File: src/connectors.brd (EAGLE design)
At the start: 37.8 x 13.4 mm, 11 parts, among them CON1 CON-4P-TABS-JST_GH-RA, CON11 PINHEAD_1X03-2, CON12 PINHEAD_1X03-2, CON3 CON-4P-TABS-JST_GH-RA, IC6 TJA1051-HVSON8, IC8 TPD3S014DBVR-SOT23-6

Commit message: Updates here and there
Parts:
- moved CON11 0.90 mm to (16.8, -3.90)
- moved CON12 0.90 mm to (-16.8, -3.90)
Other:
- board size 37.8 x 13.4 mm -> 36 x 13.4 mm
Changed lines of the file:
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@@
 <setting verticaltext="up"/>
 </settings>
-<grid distance="0.1" unitdist="mm" unit="mm" style="lines" multiple="1" display="yes" altdistance="5" altunitdist="mil" altunit="mil"/>
+<grid distance="0.3" unitdist="mm" unit="mm" style="lines" multiple="1" display="yes" altdistance="5" altunitdist="mil" altunit="mil"/>
 <layers>
 <layer number="1" name="Top" color="4" fill="1" visible="yes" active="yes"/>
@@
 <layer number="14" name="Route14" color="22" fill="1" visible="no" active="no"/>
 <layer number="15" name="Route15" color="23" fill="1" visible="no" active="no"/>
-<layer number="16" name="Bottom" color="1" fill="1" visible="yes" active="yes"/>
+<layer number="16" name="Bottom" color="1" fill="1" visible="no" active="yes"/>
 <layer number="17" name="Pads" color="2" fill="1" visible="yes" active="yes"/>
 <layer number="18" name="Vias" color="2" fill="1" visible="yes" active="yes"/>
@@
 <layer number="20" name="Dimension" color="24" fill="1" visible="yes" active="yes"/>
 <layer number="21" name="tPlace" color="7" fill="1" visible="yes" active="yes"/>
-<layer number="22" name="bPlace" color="7" fill="1" visible="yes" active="yes"/>
+<layer number="22" name="bPlace" color="7" fill="1" visible="no" active="yes"/>
 <layer number="23" name="tOrigins" color="15" fill="1" visible="yes" active="yes"/>
-<layer number="24" name="bOrigins" color="15" fill="1" visible="yes" active="yes"/>
+<layer number="24" name="bOrigins" color="15" fill="1" visible="no" active="yes"/>
 <layer number="25" name="tNames" color="7" fill="1" visible="yes" active="yes"/>
-<layer number="26" name="bNames" color="7" fill="1" visible="yes" active="yes"/>
+<layer number="26" name="bNames" color="7" fill="1" visible="no" active="yes"/>
 <layer number="27" name="tValues" color="7" fill="1" visible="no" active="yes"/>
 <layer number="28" name="bValues" color="7" fill="1" visible="no" active="yes"/>
@@
 <layer number="50" name="dxf" color="7" fill="1" visible="no" active="no"/>
 <layer number="51" name="tDocu" color="7" fill="1" visible="yes" active="yes"/>
-<layer number="52" name="bDocu" color="7" fill="1" visible="yes" active="yes"/>
+<layer number="52" name="bDocu" color="7" fill="1" visible="no" active="yes"/>
 <layer number="53" name="tGND_GNDA" color="7" fill="9" visible="no" active="no"/>
 <layer number="54" name="bGND_GNDA" color="1" fill="9" visible="no" active="no"/>
@@
 </layers>
 <board>
-<fusionsync huburn="a.cGVyc29uYWw6dWUyYWE4ZDY4" projecturn="a.cGVyc29uYWw6dWUyYWE4ZDY4IzIwMjAwOTI1MzM2NDYxMjgx" f3durn="urn:adsk.wipprod:dm.lineage:pbb1l4fuQAGy4r_gEChu-w" pcbguid="" lastpulledtime="" lastsyncedchangeguid="" latestrevisionid="46bfaa87-77a5-4bb5-bbbf-92cb329495d3" lastsyncedrevisionid="46bfaa87-77a5-4bb5-bbbf-92cb329495d3" lastboardhashguid="8e5156ea-7f44-40c5-9889-4eb4bba22418" lastpushedtime="2020-10-07T14:29:08Z" linktopcb3d="true"/>
+<fusionsync huburn="a.cGVyc29uYWw6dWUyYWE4ZDY4" projecturn="a.cGVyc29uYWw6dWUyYWE4ZDY4IzIwMjAwOTI1MzM2NDYxMjgx" f3durn="urn:adsk.wipprod:dm.lineage:5f-RR5beSAqgs6k1iF_brA" pcbguid="" lastpulledtime="" lastsyncedchangeguid="" latestrevisionid="91c3f639-02cc-4b84-a14b-e3aaad1c6eab" lastsyncedrevisionid="91c3f639-02cc-4b84-a14b-e3aaad1c6eab" lastboardhashguid="354a8440-501e-4556-71f2-56a415103d28" lastpushedtime="2020-10-31T23:22:11Z" linktopcb3d="false"/>
 <plain>
 <wire x1="5.5" y1="1.1" x2="5.5" y2="0.1" width="0.1524" layer="138"/>
 <wire x1="5" y1="0.6" x2="6" y2="0.6" width="0.1524" layer="138"/>
-<wire x1="-15.1" y1="6.3" x2="-15.1" y2="3.65" width="0.01" layer="20"/>
-<wire x1="-15.1" y1="3.65" x2="-17.35" y2="1.4" width="0.01" layer="20" curve="-90"/>
-<wire x1="-17.35" y1="1.4" x2="-18.9" y2="1.4" width="0.01" layer="20"/>
-<wire x1="-18.9" y1="1.4" x2="-18.9" y2="-7.1" width="0.01" layer="20"/>
-<wire x1="-18.9" y1="-7.1" x2="-15" y2="-7.1" width="0.01" layer="20"/>
-<wire x1="14.8" y1="-7.1" x2="14.8" y2="-1" width="0.01" layer="20"/>
-<wire x1="14.8" y1="-1" x2="13.8" y2="0" width="0.01" layer="20" curve="90"/>
-<wire x1="13.8" y1="0" x2="-14" y2="0" width="0.01" layer="20"/>
-<wire x1="-14" y1="0" x2="-15" y2="-1" width="0.01" layer="20" curve="90"/>
-<wire x1="-15" y1="-1" x2="-15" y2="-7.1" width="0.01" layer="20"/>
-<wire x1="-15.1" y1="6.3" x2="15.1" y2="6.3" width="0.01" layer="20"/>
-<wire x1="15.1" y1="6.3" x2="15.1" y2="3.65" width="0.01" layer="20"/>
-<wire x1="15.1" y1="3.65" x2="17.35" y2="1.4" width="0.01" layer="20" curve="90"/>
-<wire x1="17.35" y1="1.4" x2="18.9" y2="1.4" width="0.01" layer="20"/>
-<wire x1="18.9" y1="1.4" x2="18.9" y2="-7.1" width="0.01" layer="20"/>
-<wire x1="18.9" y1="-7.1" x2="14.8" y2="-7.1" width="0.01" layer="20"/>
+<wire x1="17" y1="-7.1" x2="15.6" y2="-7.1" width="0.01" layer="20"/>
+<wire x1="15.6" y1="-7.1" x2="14.6" y2="-6.1" width="0.01" layer="20" curve="-90"/>
+<wire x1="14.6" y1="-6.1" x2="14.6" y2="-1" width="0.01" layer="20"/>
+<wire x1="14.6" y1="-1" x2="13.6" y2="0" width="0.01" layer="20" curve="90"/>
+<wire x1="13.6" y1="0" x2="-13.6" y2="0" width="0.01" layer="20"/>
+<wire x1="-13.6" y1="0" x2="-14.6" y2="-1" width="0.01" layer="20" curve="90"/>
+<wire x1="-14.6" y1="-1" x2="-14.6" y2="-6.1" width="0.01" layer="20"/>
+<wire x1="-14.6" y1="-6.1" x2="-15.6" y2="-7.1" width="0.01" layer="20" curve="-90"/>
+<wire x1="-15.6" y1="-7.1" x2="-17" y2="-7.1" width="0.01" layer="20"/>
+<wire x1="-17" y1="-7.1" x2="-18" y2="-6.1" width="0.01" layer="20" curve="-90"/>
+<wire x1="-18" y1="-6.1" x2="-18" y2="5.3" width="0.01" layer="20"/>
+<wire x1="-18" y1="5.3" x2="-17" y2="6.3" width="0.01" layer="20" curve="-90"/>
+<wire x1="-17" y1="6.3" x2="17" y2="6.3" width="0.01" layer="20"/>
+<wire x1="17" y1="6.3" x2="18" y2="5.3" width="0.01" layer="20" curve="-90"/>
+<wire x1="18" y1="5.3" x2="18" y2="-6.1" width="0.01" layer="20"/>
+<wire x1="18" y1="-6.1" x2="17" y2="-7.1" width="0.01" layer="20" curve="-90"/>
 </plain>
 <attributes>
@@
 <attribute name="VOLTAGE" value="6.3V" x="-7" y="5.3" size="1.778" layer="27" rot="R90" display="off"/>
 </element>
-<element name="CON11" library="pinhead" library_urn="urn:adsk.eagle:library:2540341" package="1X03-PTH-2" package3d_urn="urn:adsk.eagle:package:4854341/3" value="PINHEAD_1X03-2" x="17.7" y="-3.9" smashed="yes" rot="R270">
-<attribute name="NAME" x="19.3" y="-3.9" size="1" layer="25" font="vector" ratio="15" rot="R270" align="center"/>
-</element>
-<element name="CON12" library="pinhead" library_urn="urn:adsk.eagle:library:2540341" package="1X03-PTH-2" package3d_urn="urn:adsk.eagle:package:4854341/3" value="PINHEAD_1X03-2" x="-17.7" y="-3.9" smashed="yes" rot="R90">
-<attribute name="NAME" x="-19.3" y="-3.9" size="1" layer="25" font="vector" ratio="15" rot="R90" align="center"/>
+<element name="CON11" library="pinhead" library_urn="urn:adsk.eagle:library:2540341" package="1X03-PTH-2" package3d_urn="urn:adsk.eagle:package:4854341/3" value="PINHEAD_1X03-2" x="16.8" y="-3.9" smashed="yes" rot="R270">
+<attribute name="NAME" x="18.4" y="-3.9" size="1" layer="25" font="vector" ratio="15" rot="R270" align="center"/>
+</element>
+<element name="CON12" library="pinhead" library_urn="urn:adsk.eagle:library:2540341" package="1X03-PTH-2" package3d_urn="urn:adsk.eagle:package:4854341/3" value="PINHEAD_1X03-2" x="-16.8" y="-3.9" smashed="yes" rot="R90">
+<attribute name="NAME" x="-18.4" y="-3.9" size="1" layer="25" font="vector" ratio="15" rot="R90" align="center"/>
 </element>
 </elements>

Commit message: connectors PCB routing effort
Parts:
- removed CON11, CON12: PINHEAD_1X03-2, pinhead:1X03-PTH-2
- added CON2: CON-4P-TABS-JST_GH-RA, Connectors:JST_GH-4P-RA
- added CON4: PINHEAD_1X04-2, pinhead:1X04-PTH-2
- CON3: value CON-4P-TABS-JST_GH-RA -> PINHEAD_1X04-2; device Connectors:JST_GH-4P-RA -> pinhead:1X04-PTH-2
- moved C84 83.5 mm to (16.9, 78.7)
- moved C28 79.2 mm to (15.7, 78.5), turned to 270 degrees
- moved IC8 78.6 mm to (15.5, 75.6), turned to 180 degrees
- moved C53 78.2 mm to (12.5, 79.1), turned to 180 degrees
- moved C29 77.9 mm to (14.4, 78.5), turned to 270 degrees
- moved IC6 74.0 mm to (11.0, 76.5), turned to 0 degrees
- moved CON1 74.0 mm to (-4.50, 78.2)
- moved C11 71.8 mm to (11.2, 74.3), turned to 180 degrees
- moved CON3 66.7 mm to (16.8, 69.8), turned to 270 degrees
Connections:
- net CAN1_RX: now also CON3.3
- net CAN1_TX: now also CON3.4
- net CAN1_VDD: now also CON2.1; no longer CON3.1
- net GND: now also CON2.4, CON2.M$0, CON2.M$1, CON3.2; no longer CON3.4, CON3.M$0, CON3.M$1
- net N$23: now also CON2.2; no longer CON3.2
- net N$25: now also CON2.3; no longer CON3.3
- net VDD_5V: now also CON3.1
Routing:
- net N$25: track 0.00 -> 26.5 mm, vias 0 -> 2
- net N$23: track 0.00 -> 22.2 mm, vias 0 -> 2
- net CAN1_TX: track 0.00 -> 17.9 mm, vias 0 -> 2
- net CAN1_RX: track 0.00 -> 13.6 mm, vias 0 -> 2
- net VDD_5V: track 0.00 -> 11.6 mm, vias 0 -> 5
- net CAN1_VDD: track 0.00 -> 6.51 mm, vias 0 -> 12
- net GND: track 0.00 -> 2.92 mm, vias 0 -> 17
- added copper zone on layer 1, net CAN1_VDD
- added copper zone on layer 16, net CAN1_VDD
- added copper zone on layer 1, net GND
- added copper zone on layer 16, net GND
- added copper zone on layer 1, net VDD_5V
- added copper zone on layer 16, net VDD_5V
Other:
- board size 36 x 13.4 mm -> 36 x 14.4 mm

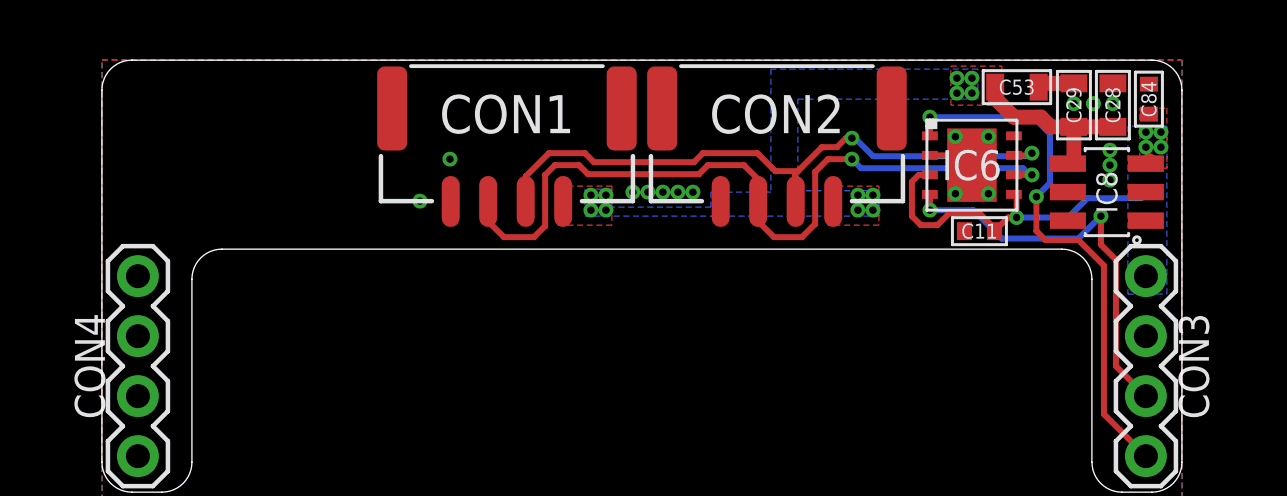
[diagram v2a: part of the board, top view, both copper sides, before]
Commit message: connectors pcb adjustments
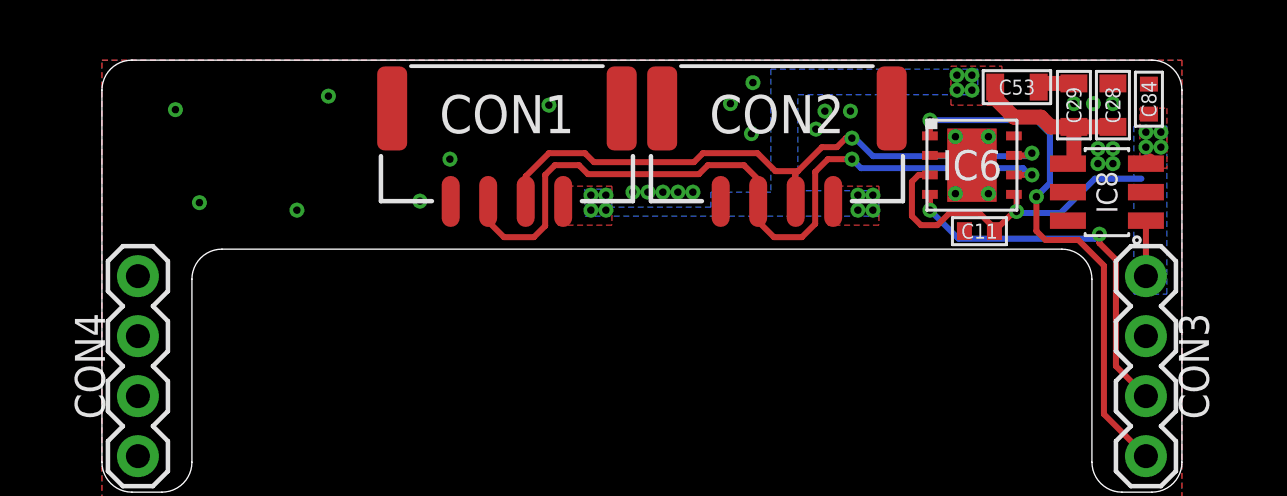
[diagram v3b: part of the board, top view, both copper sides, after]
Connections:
- removed net BEC_EN: IC8.1
- net VDD_5V: now also IC8.1
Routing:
- net VDD_5V: track 11.6 -> 13.6 mm
- net CAN1_RX: track 13.6 -> 12.7 mm
- net GND: track 2.92 -> 2.76 mm, vias 17 -> 29
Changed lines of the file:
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@@
 <vertex x="-18" y="65"/>
 </polygon>
-<wire x1="-7.29" y1="75.19" x2="-7.4" y2="75.3" width="0.2" layer="1"/>
 <via x="-7.4" y="75.3" extent="1-16" drill="0.25" diameter="0.5"/>
 <via x="-6.4" y="76.7" extent="1-16" drill="0.25" diameter="0.5"/>
@@
 <wire x1="9.6" y1="76.825" x2="10.675" y2="76.825" width="0.2" layer="1"/>
 <wire x1="10.675" y1="76.825" x2="11" y2="76.5" width="0.2" layer="1"/>
-<via x="15.6" y="77" extent="1-16" drill="0.25" diameter="0.5"/>
-<via x="15.6" y="76.5" extent="1-16" drill="0.25" diameter="0.5"/>
-<via x="15.6" y="76" extent="1-16" drill="0.25" diameter="0.5"/>
+<via x="15.7" y="77.05" extent="1-16" drill="0.25" diameter="0.5"/>
+<via x="15.7" y="76.55" extent="1-16" drill="0.25" diameter="0.5"/>
+<via x="15.2" y="76.55" extent="1-16" drill="0.25" diameter="0.5"/>
 <via x="15.7" y="78.55" extent="1-16" drill="0.25" diameter="0.5"/>
 <via x="15.05" y="78.55" extent="1-16" drill="0.25" diameter="0.5"/>
@@
 <via x="10.45" y="77.45" extent="1-16" drill="0.25" diameter="0.5"/>
 <via x="11.55" y="77.45" extent="1-16" drill="0.25" diameter="0.5"/>
-<wire x1="13.225" y1="79.1" x2="11.55" y2="77.45" width="0" layer="19" extent="1-1"/>
-<wire x1="16.8" y1="70.8" x2="16.8" y2="75.6" width="0" layer="19" extent="1-1"/>
+<via x="15.2" y="77.05" extent="1-16" drill="0.25" diameter="0.5"/>
+<via x="-10.45" y="78.8" extent="1-16" drill="0.25" diameter="0.5"/>
+<via x="-15.55" y="78.35" extent="1-16" drill="0.25" diameter="0.5"/>
+<via x="-14.75" y="75.25" extent="1-16" drill="0.25" diameter="0.5"/>
+<via x="-11.5" y="75" extent="1-16" drill="0.25" diameter="0.5"/>
+<via x="-3.1" y="78.5" extent="1-16" drill="0.25" diameter="0.5"/>
+<via x="3.7" y="79.25" extent="1-16" drill="0.25" diameter="0.5"/>
+<via x="2.95" y="78.55" extent="1-16" drill="0.25" diameter="0.5"/>
+<via x="6.1" y="78.3" extent="1-16" drill="0.25" diameter="0.5"/>
+<via x="5.8" y="77.7" extent="1-16" drill="0.25" diameter="0.5"/>
+<via x="6.95" y="78.3" extent="1-16" drill="0.25" diameter="0.5"/>
+<via x="3.65" y="77.55" extent="1-16" drill="0.25" diameter="0.5"/>
 </signal>
 <signal name="CAN1_TX">
 <contactref element="IC6" pad="1"/>
 <contactref element="CON3" pad="4"/>
-<wire x1="9.6" y1="77.475" x2="9.6" y2="78.1" width="0.2" layer="1"/>
-<via x="9.6" y="78.1" extent="1-16" drill="0.25" diameter="0.5"/>
+<wire x1="9.6" y1="77.475" x2="9.6" y2="78" width="0.2" layer="1"/>
+<via x="9.6" y="78" extent="1-16" drill="0.25" diameter="0.5"/>
 <wire x1="16.8" y1="66.8" x2="15.4" y2="68.2" width="0.2" layer="1"/>
 <wire x1="15.4" y1="68.2" x2="15.4" y2="73.15259375" width="0.2" layer="1"/>
@@
 <via x="13.15" y="75.45" extent="1-16" drill="0.25" diameter="0.5"/>
 <wire x1="13.15" y1="75.45" x2="13.6" y2="75.9" width="0.2" layer="16"/>
-<wire x1="13.05" y1="78.1" x2="9.6" y2="78.1" width="0.2" layer="16"/>
+<wire x1="13.15" y1="78" x2="9.6" y2="78" width="0.2" layer="16"/>
 <wire x1="13.6" y1="75.9" x2="13.6" y2="77.55" width="0.2" layer="16"/>
-<wire x1="13.6" y1="77.55" x2="13.05" y2="78.1" width="0.2" layer="16"/>
+<wire x1="13.6" y1="77.55" x2="13.15" y2="78" width="0.2" layer="16"/>
 </signal>
 <signal name="CAN1_RX">
@@
 <via x="9.6" y="75" extent="1-16" drill="0.25" diameter="0.5"/>
 <wire x1="16.8" y1="68.8" x2="15.8" y2="69.8" width="0.2" layer="1"/>
-<wire x1="15.8" y1="73.35" x2="15.3" y2="73.85" width="0.2" layer="1"/>
-<wire x1="15.3" y1="73.85" x2="15.3" y2="74.8" width="0.2" layer="1"/>
-<via x="15.3" y="74.8" extent="1-16" drill="0.25" diameter="0.5"/>
+<wire x1="15.8" y1="73.35" x2="15.25" y2="73.9" width="0.2" layer="1"/>
+<wire x1="15.25" y1="73.9" x2="15.25" y2="74.2" width="0.2" layer="1"/>
+<via x="15.25" y="74.2" extent="1-16" drill="0.25" diameter="0.5"/>
 <wire x1="15.8" y1="69.8" x2="15.8" y2="73.35" width="0.2" layer="1"/>
-<wire x1="15.3" y1="74.8" x2="14.55" y2="74.05" width="0.2" layer="16"/>
-<wire x1="14.55" y1="74.05" x2="12" y2="74.05" width="0.2" layer="16"/>
-<wire x1="12" y1="74.05" x2="11.05" y2="75" width="0.2" layer="16"/>
-<wire x1="11.05" y1="75" x2="9.6" y2="75" width="0.2" layer="16"/>
+<wire x1="15.25" y1="74.2" x2="15.1" y2="74.05" width="0.2" layer="16"/>
+<wire x1="15.1" y1="74.05" x2="10.55" y2="74.05" width="0.2" layer="16"/>
+<wire x1="10.55" y1="74.05" x2="9.6" y2="75" width="0.2" layer="16"/>
 </signal>
 <signal name="N$23">
@@
 <polygon width="0.2" layer="16" thermals="no">
 <vertex x="17.5" y="77.8"/>
-<vertex x="16.2" y="77.8"/>
-<vertex x="16.2" y="72.2"/>
+<vertex x="16.4" y="77.8"/>
+<vertex x="16.4" y="72.2"/>
 <vertex x="17.5" y="72.2"/>
 </polygon>
@@
 <wire x1="10.25" y1="74.9" x2="11.25" y2="74.9" width="0.2" layer="1"/>
 <wire x1="11.75" y1="74.3" x2="11.85" y2="74.3" width="0.2" layer="1"/>
-<via x="12.4878875" y="74.755" extent="1-16" drill="0.25" diameter="0.5"/>
+<via x="12.4878875" y="74.955" extent="1-16" drill="0.25" diameter="0.5"/>
 <wire x1="11.25" y1="74.9" x2="11.85" y2="74.3" width="0.2" layer="1"/>
-<wire x1="11.75" y1="74.3" x2="12.205" y2="74.755" width="0.2" layer="1"/>
-<wire x1="12.205" y1="74.755" x2="12.4878875" y2="74.755" width="0.2" layer="1"/>
+<wire x1="11.75" y1="74.3" x2="12.405" y2="74.955" width="0.2" layer="1"/>
+<wire x1="12.405" y1="74.955" x2="12.4878875" y2="74.955" width="0.2" layer="1"/>
 <wire x1="12.4" y1="75.525" x2="12.4878875" y2="75.4371125" width="0.2" layer="1"/>
-<wire x1="12.4878875" y1="75.4371125" x2="12.4878875" y2="74.755" width="0.2" layer="1"/>
-<wire x1="12.4878875" y1="74.755" x2="14.205" y2="74.755" width="0.2" layer="16"/>
-<wire x1="14.205" y1="74.755" x2="14.85" y2="75.4" width="0.2" layer="16"/>
-<wire x1="14.85" y1="75.4" x2="16.65" y2="75.4" width="0.2" layer="16"/>
+<wire x1="12.4878875" y1="75.4371125" x2="12.4878875" y2="74.955" width="0.2" layer="1"/>
+<wire x1="12.4878875" y1="74.955" x2="12.5378875" y2="74.905" width="0.2" layer="16"/>
+<wire x1="13.955" y1="74.905" x2="12.5378875" y2="74.905" width="0.2" layer="16"/>
+<wire x1="13.955" y1="74.905" x2="15.1" y2="76.05" width="0.2" layer="16"/>
+<wire x1="15.1" y1="76.05" x2="16.65" y2="76.05" width="0.2" layer="16"/>
+<contactref element="IC8" pad="1"/>
+<wire x1="16.8" y1="74.65" x2="16.8" y2="72.8" width="0.2" layer="1"/>
 </signal>
 <signal name="CAN1_VDD">
@@
 <vertex x="7.9" y="75.65"/>
 <vertex x="5.2" y="75.65"/>
-<vertex x="5.2" y="78.7"/>
-<vertex x="11.2" y="78.7"/>
+<vertex x="5.2" y="78.85"/>
+<vertex x="11.2" y="78.85"/>
 <vertex x="11.2" y="79.7"/>
 <vertex x="4.3" y="79.7"/>
@@
 <vertex x="12" y="79.8"/>
 </polygon>
-<via x="11" y="78.9" extent="1-16" drill="0.25" diameter="0.5"/>
-<via x="10.5" y="78.9" extent="1-16" drill="0.25" diameter="0.5"/>
-<via x="11" y="79.4" extent="1-16" drill="0.25" diameter="0.5"/>
-<via x="10.5" y="79.4" extent="1-16" drill="0.25" diameter="0.5"/>
+<via x="11" y="79" extent="1-16" drill="0.25" diameter="0.5"/>
+<via x="10.5" y="79" extent="1-16" drill="0.25" diameter="0.5"/>
+<via x="11" y="79.5" extent="1-16" drill="0.25" diameter="0.5"/>
+<via x="10.5" y="79.5" extent="1-16" drill="0.25" diameter="0.5"/>
 <wire x1="15.7" y1="77.775" x2="14.4" y2="77.775" width="0.5" layer="1"/>
 <wire x1="14.4" y1="77.775" x2="14.4" y2="76.55" width="0.5" layer="1"/>
@@
 <wire x1="11.775" y1="78.725" x2="11.775" y2="79.1" width="0.5" layer="1"/>
 </signal>
-<signal name="BEC_EN">
-<contactref element="IC8" pad="1"/>
-</signal>
 </signals>
